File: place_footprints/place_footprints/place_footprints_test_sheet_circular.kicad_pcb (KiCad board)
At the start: 2 copper layers, 64 parts

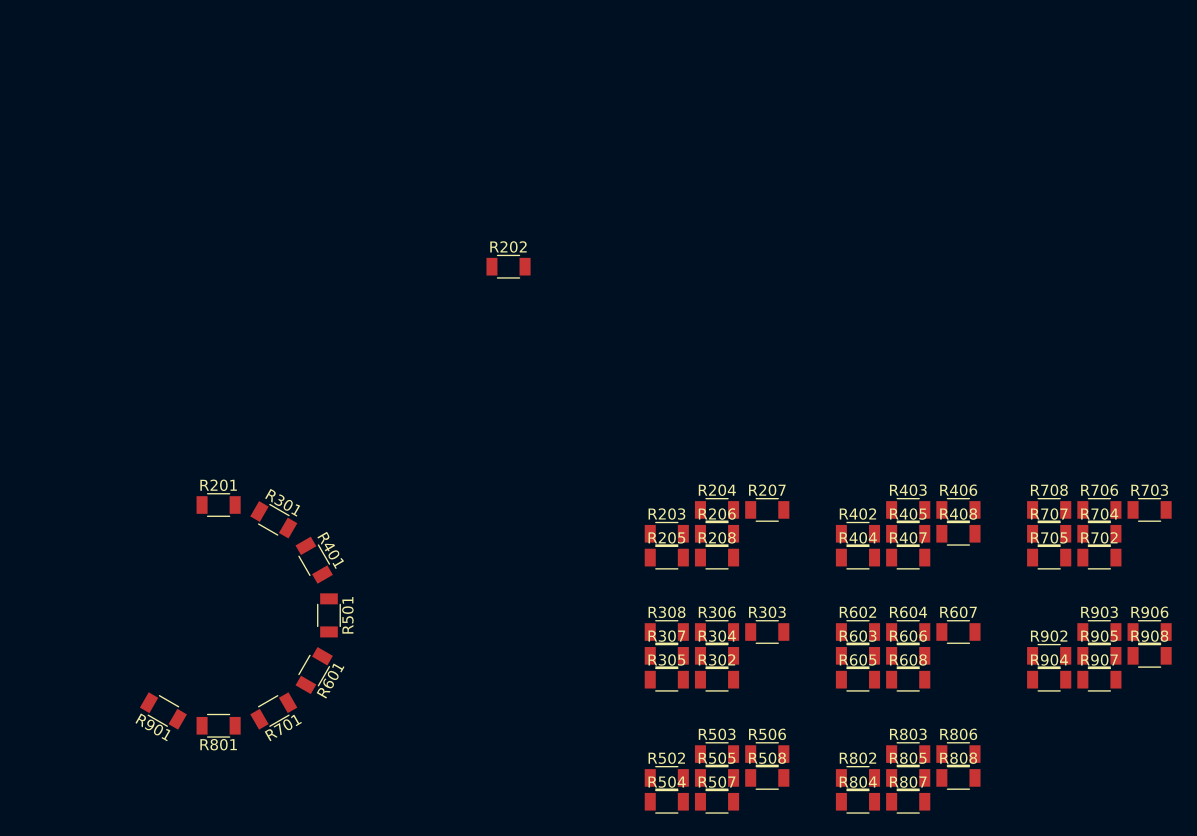
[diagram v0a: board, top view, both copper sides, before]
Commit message: Fixed circular placement
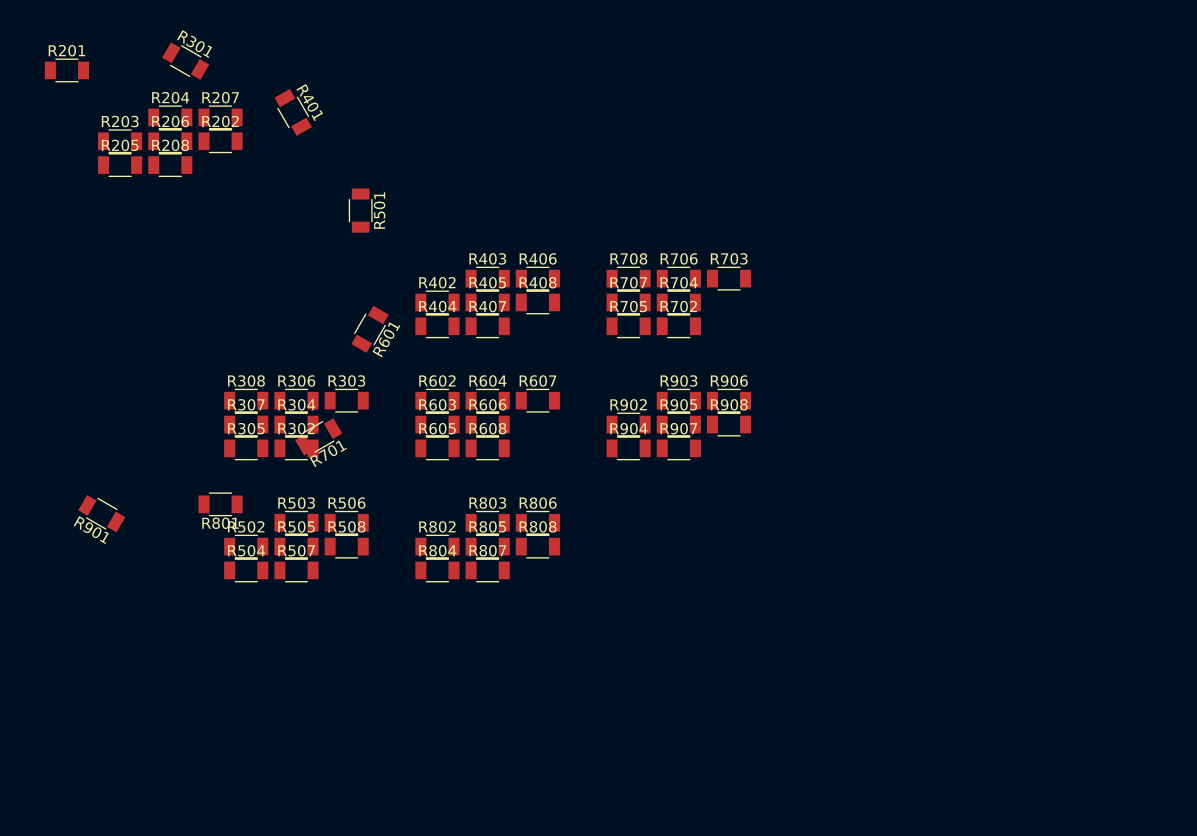
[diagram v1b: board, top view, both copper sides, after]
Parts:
- moved R204 61.0 mm to (53.2, 33.5)
- moved R206 61.0 mm to (53.2, 35.6)
- moved R208 61.0 mm to (53.2, 37.8)
- moved R207 61.0 mm to (57.7, 33.5)
- moved R203 61.0 mm to (48.6, 35.6)
- moved R205 61.0 mm to (48.6, 37.8)
- moved R302 43.5 mm to (64.6, 63.5)
- moved R303 43.5 mm to (69.2, 59.1)
- moved R304 43.5 mm to (64.6, 61.3)
- moved R306 43.5 mm to (64.6, 59.1)
- moved R402 43.5 mm to (77.4, 50.2)
- moved R404 43.5 mm to (77.4, 52.4)
- moved R503 43.5 mm to (64.6, 70.2)
- moved R505 43.5 mm to (64.6, 72.4)
- moved R506 43.5 mm to (69.2, 70.2)
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
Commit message: added support for any footprint to serve as a reference in linear and circular mode
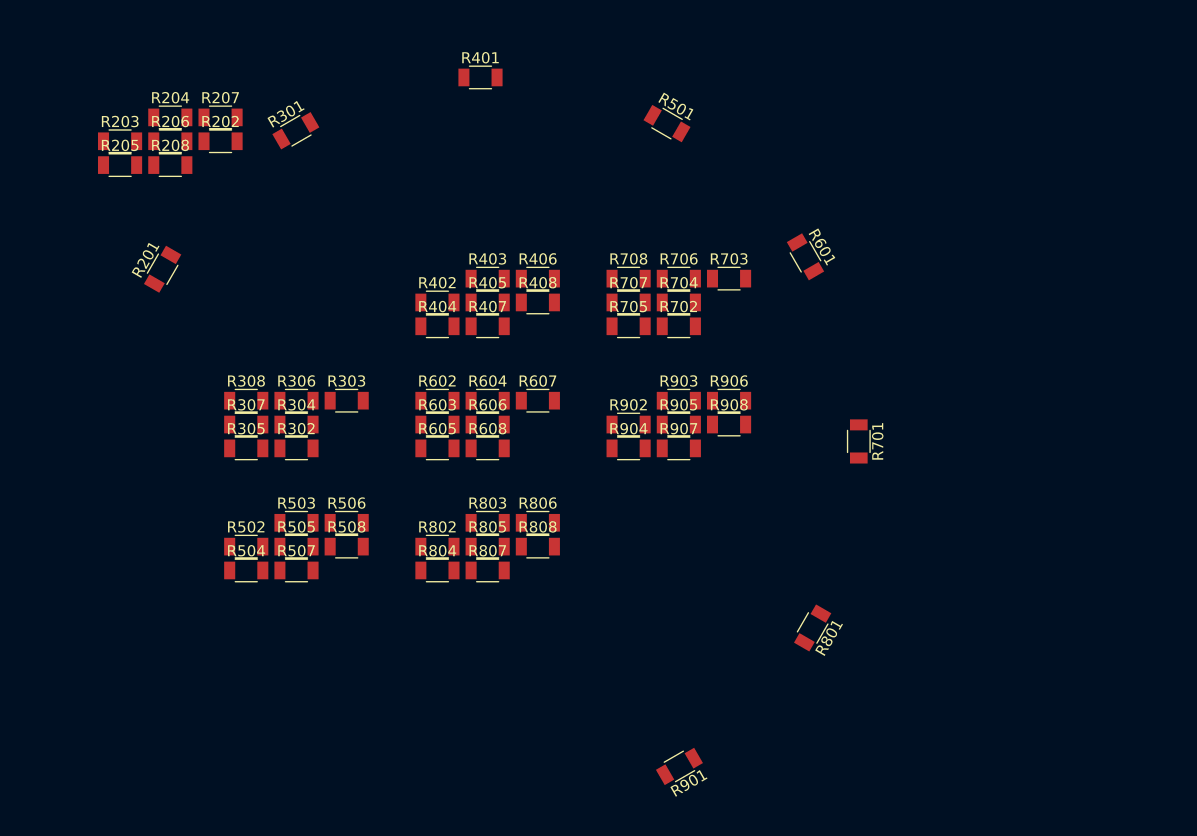
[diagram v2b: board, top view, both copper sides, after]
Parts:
- moved R901 57.1 mm to (99.3, 92.3), turned to 210 degrees
- moved R801 54.8 mm to (111.4, 79.7), turned to 240 degrees
- moved R701 48.9 mm to (115.6, 62.8), turned to 270 degrees
- moved R601 40.0 mm to (110.7, 46.1), turned to 300 degrees
- moved R501 28.8 mm to (98.2, 34.0), turned to 330 degrees
- moved R201 20.0 mm to (52.5, 47.2), turned to 60 degrees
- moved R401 17.3 mm to (81.3, 29.8), turned to 0 degrees
- moved R301 11.8 mm to (64.6, 34.7), turned to 30 degrees

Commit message: updated test cases
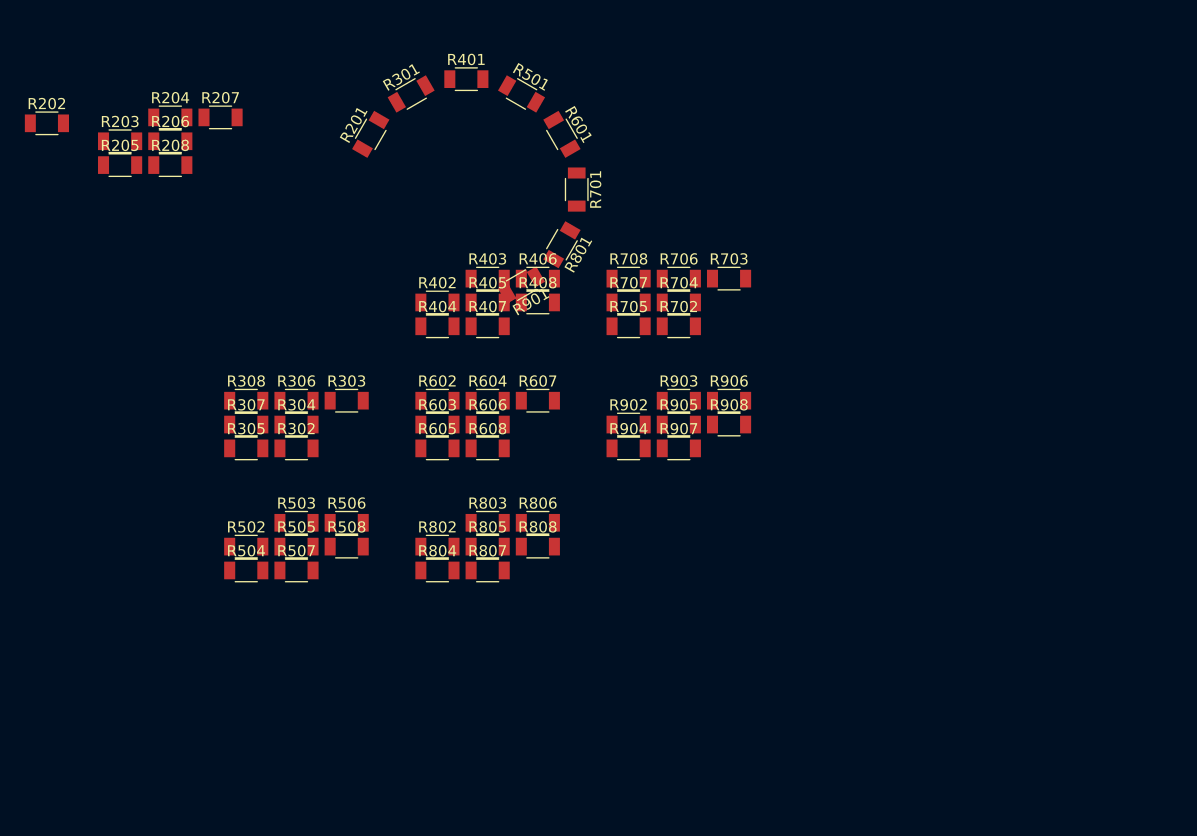
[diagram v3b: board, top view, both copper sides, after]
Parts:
- moved R901 45.9 mm to (85.0, 48.7)
- moved R801 41.5 mm to (88.7, 45.0)
- moved R701 34.3 mm to (90.0, 40.0)
- moved R601 24.7 mm to (88.7, 35.0)
- moved R201 22.5 mm to (71.3, 35.0)
- moved R202 15.8 mm to (42.0, 34.0)
- moved R501 13.5 mm to (85.0, 31.3)
- moved R301 11.0 mm to (75.0, 31.3)
- moved R401 1.29 mm to (80.0, 30.0)
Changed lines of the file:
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@@
-(kicad_pcb (version 20171130) (host pcbnew "(5.1.0-rc2-4-g73f0b3087)")
+(kicad_pcb (version 20171130) (host pcbnew "(5.1.5-90-g5c7ac1bb7)-1")
   (general
     (thickness 1.6)
@@
   )
   (module Passives:R1206M (layer F.Cu)
-    (at 98.179584 34.024895 330)
+    (at 85 31.339745 330)
     (descr "Capacitor SMD 1206, reflow soldering, AVX (see smccp.pdf)")
     (tags "capacitor 1206")
@@
   )
   (module Passives:R1206M (layer F.Cu)
-    (at 52.484894 47.220418 60)
+    (at 71.339745 35 60)
     (descr "Capacitor SMD 1206, reflow soldering, AVX (see smccp.pdf)")
     (tags "capacitor 1206")
@@
   )
   (module Passives:R1206M (layer F.Cu)
-    (at 64.554582 34.674896 30)
+    (at 75 31.339745 30)
     (descr "Capacitor SMD 1206, reflow soldering, AVX (see smccp.pdf)")
     (tags "capacitor 1206")
@@
   )
   (module Passives:R1206M (layer F.Cu)
-    (at 57.730001 35.625001)
+    (at 42 34)
     (descr "Capacitor SMD 1206, reflow soldering, AVX (see smccp.pdf)")
     (tags "capacitor 1206")
@@
   )
   (module Passives:R1206M (layer F.Cu)
-    (at 81.28 29.845)
+    (at 80 30)
     (descr "Capacitor SMD 1206, reflow soldering, AVX (see smccp.pdf)")
     (tags "capacitor 1206")
@@
   )
   (module Passives:R1206M (layer F.Cu)
-    (at 99.305419 92.265107 210)
+    (at 85 48.660254 210)
     (descr "Capacitor SMD 1206, reflow soldering, AVX (see smccp.pdf)")
     (tags "capacitor 1206")
@@
   )
   (module Passives:R1206M (layer F.Cu)
-    (at 110.725106 46.094583 300)
+    (at 88.660254 35 300)
     (descr "Capacitor SMD 1206, reflow soldering, AVX (see smccp.pdf)")
     (tags "capacitor 1206")
@@
   )
   (module Passives:R1206M (layer F.Cu)
-    (at 115.555003 62.820001 270)
+    (at 90 40 270)
     (descr "Capacitor SMD 1206, reflow soldering, AVX (see smccp.pdf)")
     (tags "capacitor 1206")
@@
   )
   (module Passives:R1206M (layer F.Cu)
-    (at 111.375107 79.719585 240)
-    (descr "Capacitor SMD 1206, reflow soldering, AVX (see smccp.pdf)")
-    (tags "capacitor 1206")
+    (at 88.660254 45 240)
+    (descr "Capacitor SMD 1206, reflow soldering, AVX (see smccp.pdf)")
+    (tags "capacitor 1206")
